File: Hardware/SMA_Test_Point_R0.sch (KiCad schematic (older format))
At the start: 2 parts

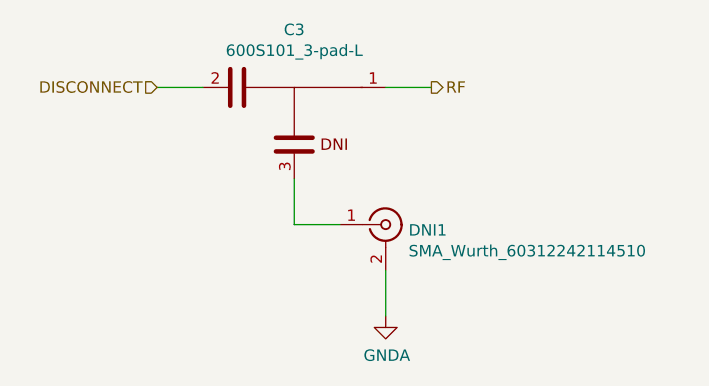
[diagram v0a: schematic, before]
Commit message: Improving LNA simulations and Documentation package. More to come on this one.
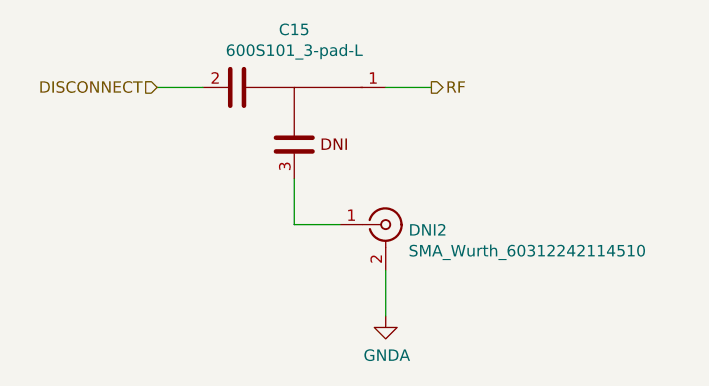
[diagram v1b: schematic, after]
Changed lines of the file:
@@
 $Descr A4 11693 8268
 encoding utf-8
-Sheet 4 24
+Sheet 7 23
 Title ""
 Date ""
@@
 AR Path="/5F204DEC/5F205D8E/5F1AED07/5F1E0C52/5F1B349C" Ref="DNI?"  Part="1"
 AR Path="/5F204DEC/5F205D8E/5F1BF90D/5F1B349C" Ref="DNI5"  Part="1"
-F 0 "DNI1" H 6150 4125 50  0000 L CNN
+F 0 "DNI2" H 6150 4125 50  0000 L CNN
 F 1 "SMA_Wurth_60312242114510" H 6150 4034 50  0000 L CNN
 F 2 "RF:SMA_Wurth_60312242114510" H 6050 4150 50  0001 C CNN
@@
 AR Path="/5F2751D2/5F1B34A3" Ref="#PWR?"  Part="1"
 AR Path="/5F20A94F/5F1AEEB1/5F1B34A3" Ref="#PWR07"  Part="1"
-AR Path="/5F20DB0B/5F1AEEB1/5F1B34A3" Ref="#PWR016"  Part="1"
+AR Path="/5F20DB0B/5F1AEEB1/5F1B34A3" Ref="#PWR018"  Part="1"
 AR Path="/5F04F5B6/5F1AED07/5F1E0C52/5F1B34A3" Ref="#PWR?"  Part="1"
 AR Path="/5F204DEC/5F205D8E/5F1AED07/5F1E0C52/5F1B34A3" Ref="#PWR?"  Part="1"
-AR Path="/5F204DEC/5F205D8E/5F1BF90D/5F1B34A3" Ref="#PWR052"  Part="1"
-F 0 "#PWR052" H 6050 4300 50  0001 C CNN
+AR Path="/5F204DEC/5F205D8E/5F1BF90D/5F1B34A3" Ref="#PWR054"  Part="1"
+F 0 "#PWR018" H 6050 4300 50  0001 C CNN
 F 1 "GNDA" H 6055 4377 50  0000 C CNN
 F 2 "" H 6050 4550 50  0001 C CNN
@@
 AR Path="/5F20A94F/5F1B34AB" Ref="C?"  Part="1"
 AR Path="/5F20A94F/5F1AEEB1/5F1B34AB" Ref="C3"  Part="1"
-AR Path="/5F20DB0B/5F1AEEB1/5F1B34AB" Ref="C12"  Part="1"
+AR Path="/5F20DB0B/5F1AEEB1/5F1B34AB" Ref="C15"  Part="1"
 AR Path="/5F04F5B6/5F1AED07/5F1E0C52/5F1B34AB" Ref="C?"  Part="1"
 AR Path="/5F204DEC/5F205D8E/5F1AED07/5F1E0C52/5F1B34AB" Ref="C?"  Part="1"
-AR Path="/5F204DEC/5F205D8E/5F1BF90D/5F1B34AB" Ref="C44"  Part="1"
-F 0 "C3" H 5650 3298 50  0000 C CNN
+AR Path="/5F204DEC/5F205D8E/5F1BF90D/5F1B34AB" Ref="C47"  Part="1"
+F 0 "C15" H 5650 3298 50  0000 C CNN
 F 1 "600S101_3-pad-L" H 5650 3389 50  0000 C CNN
 F 2 "Capacitor_SMD:C_0603_1608Metric_3-pad-L" H 6550 2800 50  0001 C CNN
